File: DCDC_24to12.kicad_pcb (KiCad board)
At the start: 2 copper layers, 61.6 x 36.7 mm, 28 parts, among them J1 Power_IN, J2 Power_OUT, U1 BD9F800MUX-ZE2

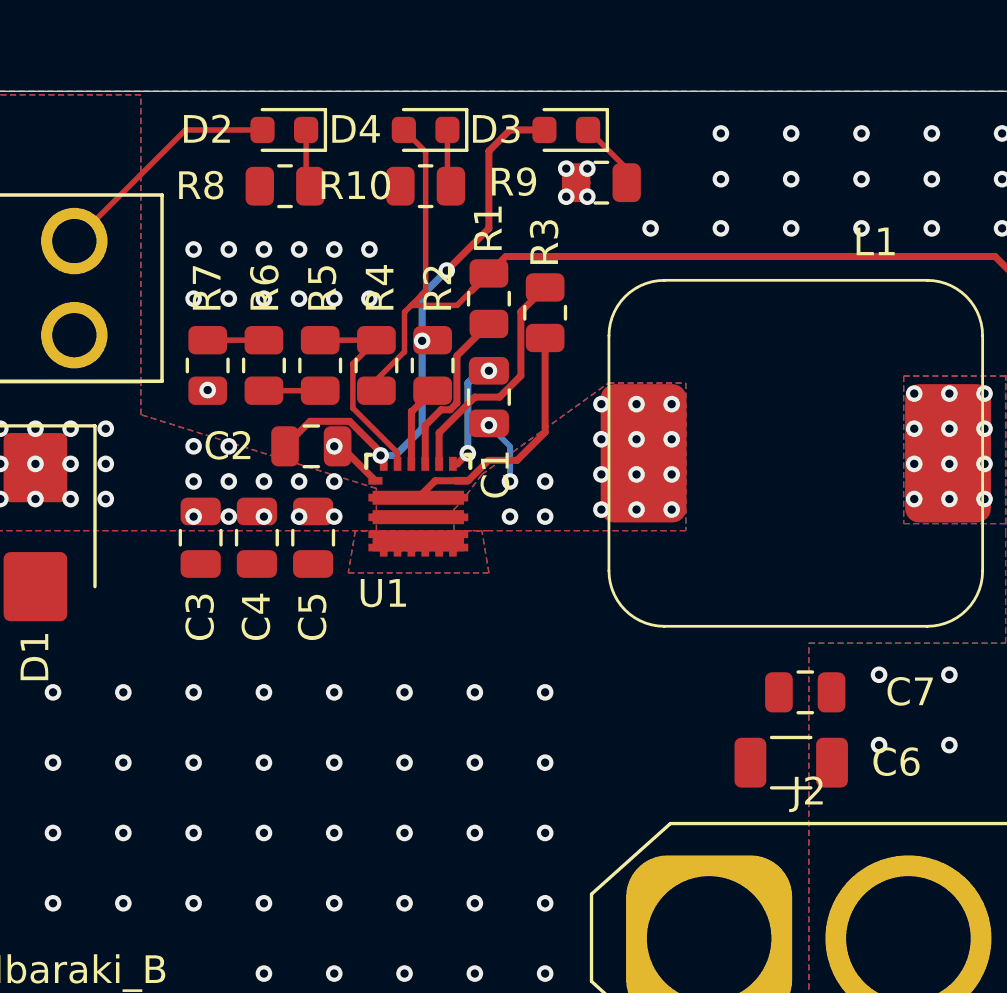
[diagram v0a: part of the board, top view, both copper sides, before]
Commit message: 抵抗配置修正、シルク調整
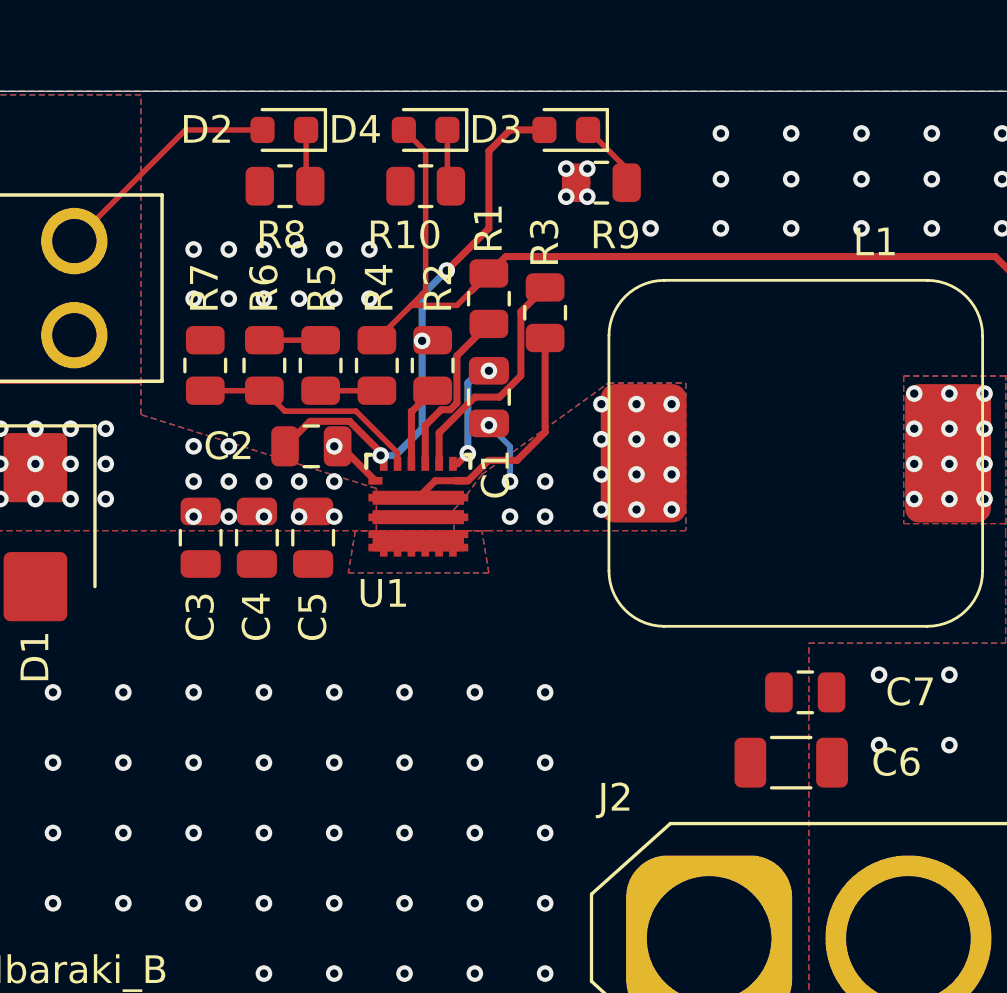
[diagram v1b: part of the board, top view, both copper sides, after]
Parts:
- moved R7 6.18 mm to (94.4, 49.1), turned to 90 degrees
- moved R5 2.05 mm to (98.6, 49.1)
- moved R6 2.05 mm to (96.5, 49.1)
- moved R4 2.05 mm to (100.6, 49.1)
- renumbered R5 to R4, R6 to R5, R7 to R6, R4 to R7
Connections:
- R4 pad 2: FB -> +12V
- R6 pad 1: GND -> FB
- R7 pad 2: +12V -> GND
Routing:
- net +12V: track 37.5 -> 35.8 mm
- net FB: track 7.52 -> 8.28 mm
- net GND: vias 108 -> 107
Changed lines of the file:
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@@
 	(net 14 "VREG")
 	(net 15 "PGD")
-	(net 16 "Net-(R6-Pad1)")
+	(net 16 "Net-(R4-Pad1)")
 	(net 17 "unconnected-(H1-Pad1)")
 	(net 18 "unconnected-(H1-Pad1)_0")
@@
 	(footprint "Resistor_SMD:R_0805_2012Metric"
 		(layer "F.Cu")
-		(at 94.488 49.149 90)
+		(at 96.536 49.149 90)
 		(descr "Resistor SMD 0805 (2012 Metric), square (rectangular) end terminal, IPC_7351 nominal, (Body size source: IPC-SM-782 page 72, https://www.pcb-3d.com/wordpress/wp-content/uploads/ipc-sm-782a_amendment_1_and_2.pdf), generated with kicad-footprint-generator")
 		(tags "resistor")
-		(property "Reference" "R7"
+		(property "Reference" "R6"
 			(at 2.794 0 90)
 			(layer "F.SilkS")
@@
 			(layers "F.Cu" "F.Paste" "F.Mask")
 			(roundrect_rratio 0.243902)
-			(net 1 "GND")
+			(net 11 "FB")
 			(pintype "passive")
 		)
@@
 			(layers "F.Cu" "F.Paste" "F.Mask")
 			(roundrect_rratio 0.243902)
-			(net 16 "Net-(R6-Pad1)")
+			(net 7 "Net-(R5-Pad1)")
 			(pintype "passive")
 		)
@@
 		(tags "resistor")
 		(property "Reference" "R9"
-			(at 3.175 0 0)
+			(at -0.508 -1.905 0)
 			(layer "F.SilkS")
 			(effects
@@
 		(tags "XT60 female vertical")
 		(property "Reference" "J2"
-			(at 3.6 -5.3 0)
+			(at -3.385 -5.08 0)
 			(layer "F.SilkS")
 			(effects
@@
 	(footprint "Resistor_SMD:R_0805_2012Metric"
 		(layer "F.Cu")
-		(at 98.552 49.149 90)
+		(at 100.6 49.149 90)
 		(descr "Resistor SMD 0805 (2012 Metric), square (rectangular) end terminal, IPC_7351 nominal, (Body size source: IPC-SM-782 page 72, https://www.pcb-3d.com/wordpress/wp-content/uploads/ipc-sm-782a_amendment_1_and_2.pdf), generated with kicad-footprint-generator")
 		(tags "resistor")
-		(property "Reference" "R5"
+		(property "Reference" "R4"
 			(at 2.794 0.1016 90)
 			(layer "F.SilkS")
@@
 			(layers "F.Cu" "F.Paste" "F.Mask")
 			(roundrect_rratio 0.243902)
-			(net 7 "Net-(R5-Pad1)")
+			(net 16 "Net-(R4-Pad1)")
 			(pintype "passive")
 		)
@@
 			(layers "F.Cu" "F.Paste" "F.Mask")
 			(roundrect_rratio 0.243902)
-			(net 11 "FB")
+			(net 2 "+12V")
 			(pintype "passive")
 		)
@@
 		(tags "resistor")
 		(property "Reference" "R10"
-			(at 2.54 0 0)
+			(at 0.762 -1.778 0)
 			(layer "F.SilkS")
 			(effects
@@
 	(footprint "Resistor_SMD:R_0805_2012Metric"
 		(layer "F.Cu")
-		(at 96.52 49.149 -90)
+		(at 98.568 49.149 -90)
 		(descr "Resistor SMD 0805 (2012 Metric), square (rectangular) end terminal, IPC_7351 nominal, (Body size source: IPC-SM-782 page 72, https://www.pcb-3d.com/wordpress/wp-content/uploads/ipc-sm-782a_amendment_1_and_2.pdf), generated with kicad-footprint-generator")
 		(tags "resistor")
-		(property "Reference" "R6"
+		(property "Reference" "R5"
 			(at -2.794 -0.0508 90)
 			(layer "F.SilkS")
@@
 			(layers "F.Cu" "F.Paste" "F.Mask")
 			(roundrect_rratio 0.243902)
-			(net 16 "Net-(R6-Pad1)")
+			(net 7 "Net-(R5-Pad1)")
 			(pintype "passive")
 		)
@@
 			(layers "F.Cu" "F.Paste" "F.Mask")
 			(roundrect_rratio 0.243902)
-			(net 7 "Net-(R5-Pad1)")
+			(net 16 "Net-(R4-Pad1)")
 			(pintype "passive")
 		)
@@
 	(footprint "Resistor_SMD:R_0805_2012Metric"
 		(layer "F.Cu")
-		(at 100.584 49.149 -90)
+		(at 94.4 49.149 90)
 		(descr "Resistor SMD 0805 (2012 Metric), square (rectangular) end terminal, IPC_7351 nominal, (Body size source: IPC-SM-782 page 72, https://www.pcb-3d.com/wordpress/wp-content/uploads/ipc-sm-782a_amendment_1_and_2.pdf), generated with kicad-footprint-generator")
 		(tags "resistor")
-		(property "Reference" "R4"
-			(at -2.794 -0.1524 90)
+		(property "Reference" "R7"
+			(at 2.794 -0.0136 90)
 			(layer "F.SilkS")
 			(effects
@@
 		)
 		(property "Footprint" "Resistor_SMD:R_0805_2012Metric"
-			(at 0 0 -90)
+			(at 0 0 90)
 			(unlocked yes)
 			(layer "F.Fab")
@@
 		)
 		(property "Datasheet" ""
-			(at 0 0 -90)
+			(at 0 0 90)
 			(unlocked yes)
 			(layer "F.Fab")
@@
 		)
 		(property "Description" "Resistor"
-			(at 0 0 -90)
+			(at 0 0 90)
 			(unlocked yes)
 			(layer "F.Fab")
@@
 		(attr smd)
 		(fp_line
-			(start -0.227064 0.735)
-			(end 0.227064 0.735)
+			(start -0.227064 -0.735)
+			(end 0.227064 -0.735)
 			(stroke
 				(width 0.12)
@@
 		)
 		(fp_line
-			(start -0.227064 -0.735)
-			(end 0.227064 -0.735)
+			(start -0.227064 0.735)
+			(end 0.227064 0.735)
 			(stroke
 				(width 0.12)
@@
 		)
 		(fp_line
-			(start -1.68 0.95)
-			(end -1.68 -0.95)
+			(start 1.68 -0.95)
+			(end 1.68 0.95)
 			(stroke
 				(width 0.05)
@@
 		)
 		(fp_line
-			(start 1.68 0.95)
-			(end -1.68 0.95)
+			(start -1.68 -0.95)
+			(end 1.68 -0.95)
 			(stroke
 				(width 0.05)
@@
 		)
 		(fp_line
-			(start -1.68 -0.95)
-			(end 1.68 -0.95)
+			(start 1.68 0.95)
+			(end -1.68 0.95)
 			(stroke
 				(width 0.05)
@@
 		)
 		(fp_line
-			(start 1.68 -0.95)
-			(end 1.68 0.95)
+			(start -1.68 0.95)
+			(end -1.68 -0.95)
 			(stroke
 				(width 0.05)
@@
 		)
 		(fp_line
-			(start -1 0.625)
-			(end -1 -0.625)
+			(start 1 -0.625)
+			(end 1 0.625)
 			(stroke
 				(width 0.1)
@@
 		)
 		(fp_line
-			(start 1 0.625)
-			(end -1 0.625)
+			(start -1 -0.625)
+			(end 1 -0.625)
 			(stroke
 				(width 0.1)
@@
 		)
 		(fp_line
-			(start -1 -0.625)
-			(end 1 -0.625)
+			(start 1 0.625)
+			(end -1 0.625)
 			(stroke
 				(width 0.1)
@@
 		)
 		(fp_line
-			(start 1 -0.625)
-			(end 1 0.625)
+			(start -1 0.625)
+			(end -1 -0.625)
 			(stroke
 				(width 0.1)
@@
 		)
 		(pad "1" smd roundrect
-			(at -0.9125 0 270)
+			(at -0.9125 0 90)
 			(size 1.025 1.4)
 			(layers "F.Cu" "F.Paste" "F.Mask")
@@
 		)
 		(pad "2" smd roundrect
-			(at 0.9125 0 270)
+			(at 0.9125 0 90)
 			(size 1.025 1.4)
 			(layers "F.Cu" "F.Paste" "F.Mask")
 			(roundrect_rratio 0.243902)
-			(net 2 "+12V")
+			(net 1 "GND")
 			(pintype "passive")
 		)
@@
 		(tags "resistor")
 		(property "Reference" "R8"
-			(at 3.048 0 0)
+			(at 0.127 -1.778 0)
 			(layer "F.SilkS")
 			(effects
@@
 	)
 	(via
-		(at 94.488 50.038)
-		(size 0.6)
-		(drill 0.3)
-		(layers "F.Cu" "B.Cu")
-		(net 1)
-	)
-	(via
 		(at 115.57 40.767)
 		(size 0.6)
@@
 	)
 	(segment
-		(start 101.6 48.653763)
-		(end 100.388131 49.865632)
-		(width 0.2)
-		(layer "F.Cu")
-		(net 2)
-	)
-	(segment
 		(start 104.648 45.8235)
 		(end 105.2595 45.212)
@@
 	)
 	(segment
-		(start 101.84225 46.97825)
-		(end 101.6 47.2205)
-		(width 0.2)
-		(layer "F.Cu")
-		(net 2)
-	)
-	(segment
 		(start 123.825 46.101)
 		(end 123.825 50.165)
@@
 	)
 	(segment
-		(start 101.6 47.2205)
-		(end 101.6 48.653763)
-		(width 0.2)
-		(layer "F.Cu")
-		(net 2)
-	)
-	(segment
 		(start 102.362 41.4275)
 		(end 102.362 46.4585)
@@
 	)
 	(segment
+		(start 100.6 48.2205)
+		(end 101.84225 46.97825)
+		(width 0.2)
+		(layer "F.Cu")
+		(net 2)
+	)
+	(segment
 		(start 101.5745 40.64)
 		(end 102.362 41.4275)
@@
 	)
 	(segment
-		(start 100.6075 50.0615)
-		(end 100.584 50.0615)
-		(width 0.254)
+		(start 100.6 48.2365)
+		(end 100.6 48.2205)
+		(width 0.2)
 		(layer "F.Cu")
 		(net 2)
@@
 	)
 	(segment
-		(start 98.552 50.0615)
-		(end 96.52 50.0615)
+		(start 96.536 48.2365)
+		(end 98.568 48.2365)
 		(width 0.2)
 		(layer "F.Cu")
@@
 	)
 	(segment
-		(start 99.734 50.690693)
-		(end 101.347811 52.304504)
+		(start 99.843307 50.8)
+		(end 97.2745 50.8)
 		(width 0.2)
 		(layer "F.Cu")
@@
 	)
 	(segment
-		(start 99.734 49.0865)
-		(end 99.734 50.690693)
+		(start 101.347811 52.304504)
+		(end 99.843307 50.8)
 		(width 0.2)
 		(layer "F.Cu")
@@
 	)
 	(segment
-		(start 100.584 48.2365)
-		(end 98.552 48.2365)
+		(start 97.2745 50.8)
+		(end 96.536 50.0615)
 		(width 0.2)
 		(layer "F.Cu")
@@
 	)
 	(segment
-		(start 100.584 48.2365)
-		(end 99.734 49.0865)
+		(start 94.4 50.0615)
+		(end 96.536 50.0615)
 		(width 0.2)
 		(layer "F.Cu")
@@
 	)
 	(segment
-		(start 101.347811 52.304504)
-		(end 101.347811 52.705)
+		(start 101.347811 52.705)
+		(end 101.347811 52.304504)
 		(width 0.2)
 		(layer "F.Cu")
@@
 	)
 	(segment
-		(start 96.52 48.2365)
-		(end 94.488 48.2365)
+		(start 98.568 50.0615)
+		(end 100.6 50.0615)
 		(width 0.2)
 		(layer "F.Cu")
@@
 		(polygon
 			(pts
-				(xy 116.205 72.39) (xy 116.205 59.182) (xy 123.317 59.182) (xy 123.317 55.245) (xy 123.317 55.245)
-				(xy 123.317 49.53) (xy 128.905 49.53) (xy 128.905 72.39)
+				(xy 116.205 72.39) (xy 116.205 59.182) (xy 123.317 59.182) (xy 123.317 55.245) (xy 123.317 49.53)
+				(xy 128.905 49.53) (xy 128.905 72.39)
 			)
 		)

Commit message: 外形とベタとりあえず拡大
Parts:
- moved C1 60.7 mm to (149.7, 90.9)
- moved C5 60.7 mm to (143.4, 96.0)
- moved C6 60.7 mm to (160.7, 104.1)
- moved D4 60.7 mm to (147.4, 81.3)
- moved F1 60.7 mm to (128.0, 87.0)
- moved J1 60.7 mm to (125.3, 102.6)
- moved R1 60.7 mm to (149.7, 87.4)
- moved R10 60.7 mm to (147.4, 83.3)
- moved R4 60.7 mm to (145.7, 89.8)
- moved R6 60.7 mm to (141.6, 89.8)
- moved R7 60.7 mm to (139.5, 89.8)
- moved C2 60.7 mm to (143.3, 92.7)
- moved C7 60.7 mm to (161.2, 101.6)
- moved H2 60.7 mm to (174.0, 83.8)
- moved U1 60.7 mm to (147.2, 94.6)
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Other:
- board size 61.6 x 36.7 mm -> 75 x 74.4 mm

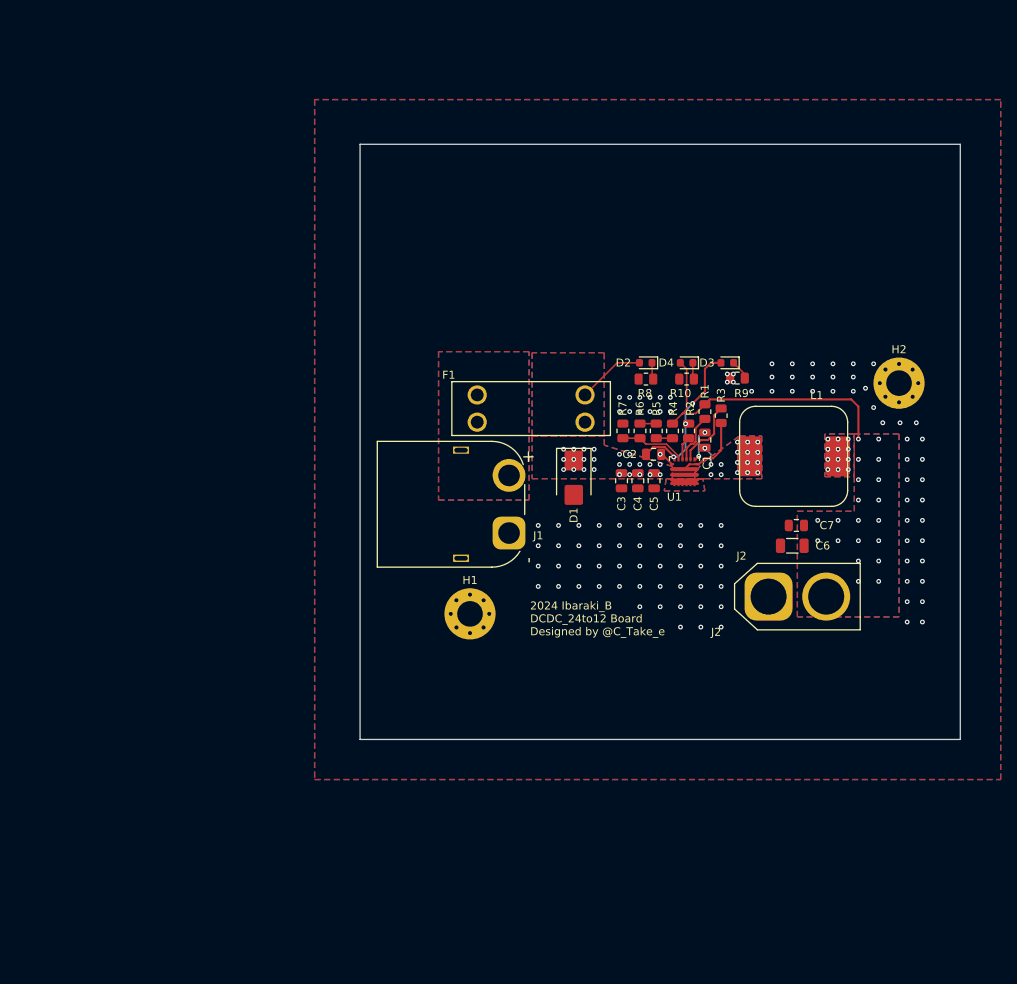
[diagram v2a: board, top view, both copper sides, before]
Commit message: 外形位置修正、ビア削除など
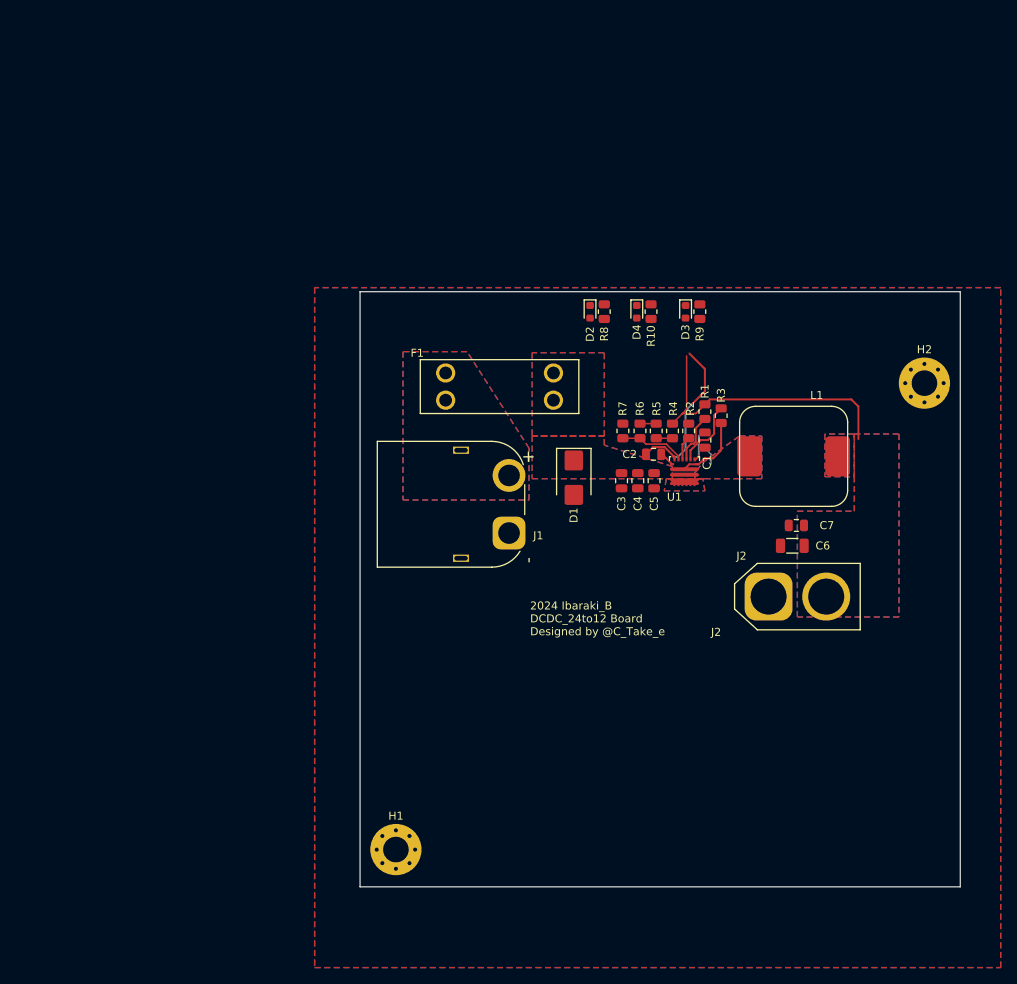
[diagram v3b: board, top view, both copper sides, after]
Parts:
- moved H1 30.9 mm to (111.1, 142.1)
- moved R8 9.91 mm to (137.2, 74.9), turned to -90 degrees
- moved R9 9.54 mm to (149.1, 74.9), turned to -90 degrees
- moved R10 9.53 mm to (143.0, 74.9), turned to -90 degrees
- moved D2 9.44 mm to (135.4, 74.9), turned to -90 degrees
- moved D4 8.91 mm to (141.2, 74.9), turned to -90 degrees
- moved D3 8.23 mm to (147.3, 74.9), turned to -90 degrees
- moved F1 4.81 mm to (124.1, 84.2)
- moved H2 3.17 mm to (177.2, 83.8)
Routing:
- net +BATT: track 17.4 -> 8.97 mm, vias 24 -> 0
- net Net-(D3-K): track 2.48 -> 0.00 mm
- net Net-(D2-K): track 2.09 -> 0.00 mm
- net Net-(D4-K): track 2.08 -> 0.00 mm
- net +12V: track 35.8 -> 36.3 mm, vias 32 -> 0
- net VREG: track 20.0 -> 20.4 mm, vias 3 -> 0
- net GND: track 2.94 -> 2.73 mm, vias 107 -> 0
- net SW: vias 17 -> 0
- net BOOT: vias 2 -> 0
